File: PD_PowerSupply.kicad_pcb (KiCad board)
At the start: 4 copper layers, 61 x 46 mm, 81 parts, among them J1 2.54mm Header, J2 Screw Terminal, Q1 STL6P3LLH6, Q2 STL6P3LLH6, U1 LM1117LD-3.3, U2 STUSB4500QTR, U3 LMR16006YQ5, U4 LTM8074IY, U5 LTC7106EDDB-1, U6 LMP92064SDE_NOPB, U7 AQV252GAX, U8 BMD-340-A-R, U9 USB6B1

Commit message: Regenerate Gerbers
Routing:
- net +5V: track 89.1 -> 88.5 mm

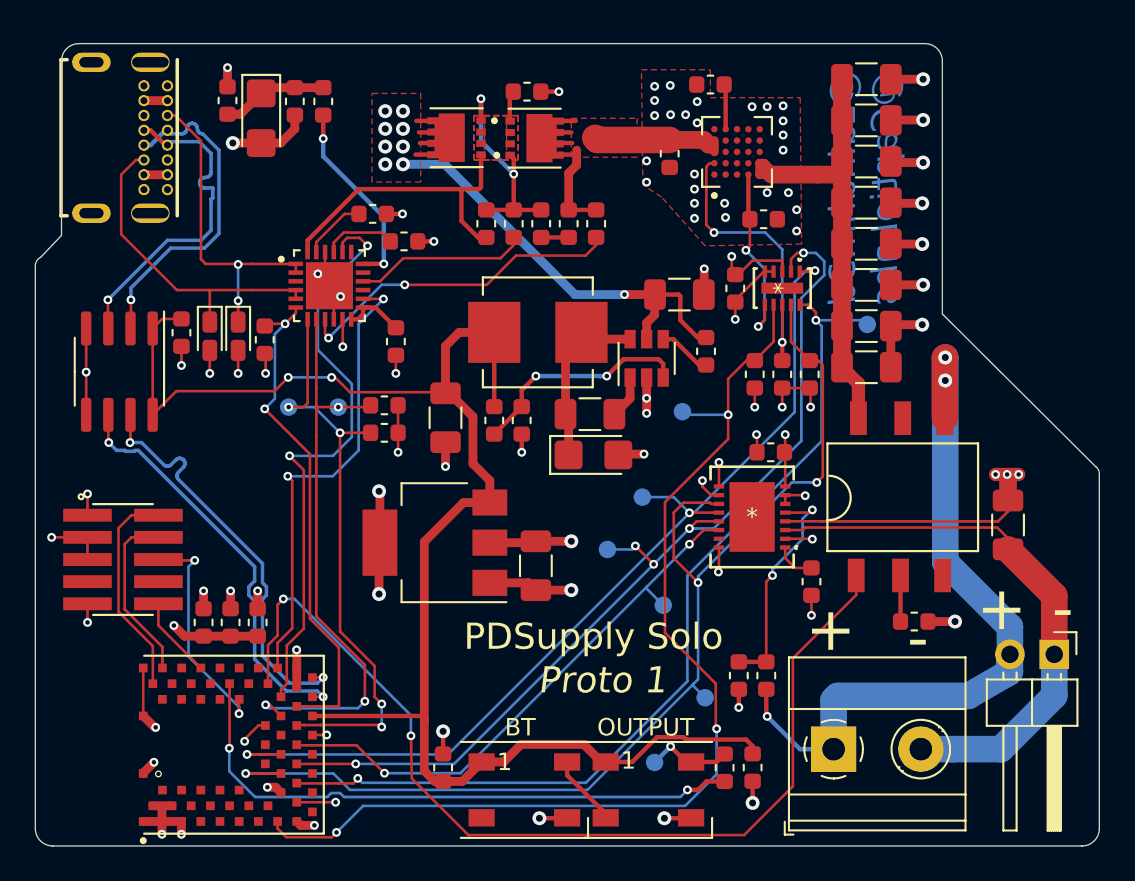
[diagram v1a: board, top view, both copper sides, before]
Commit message: Switched to PWM DAC
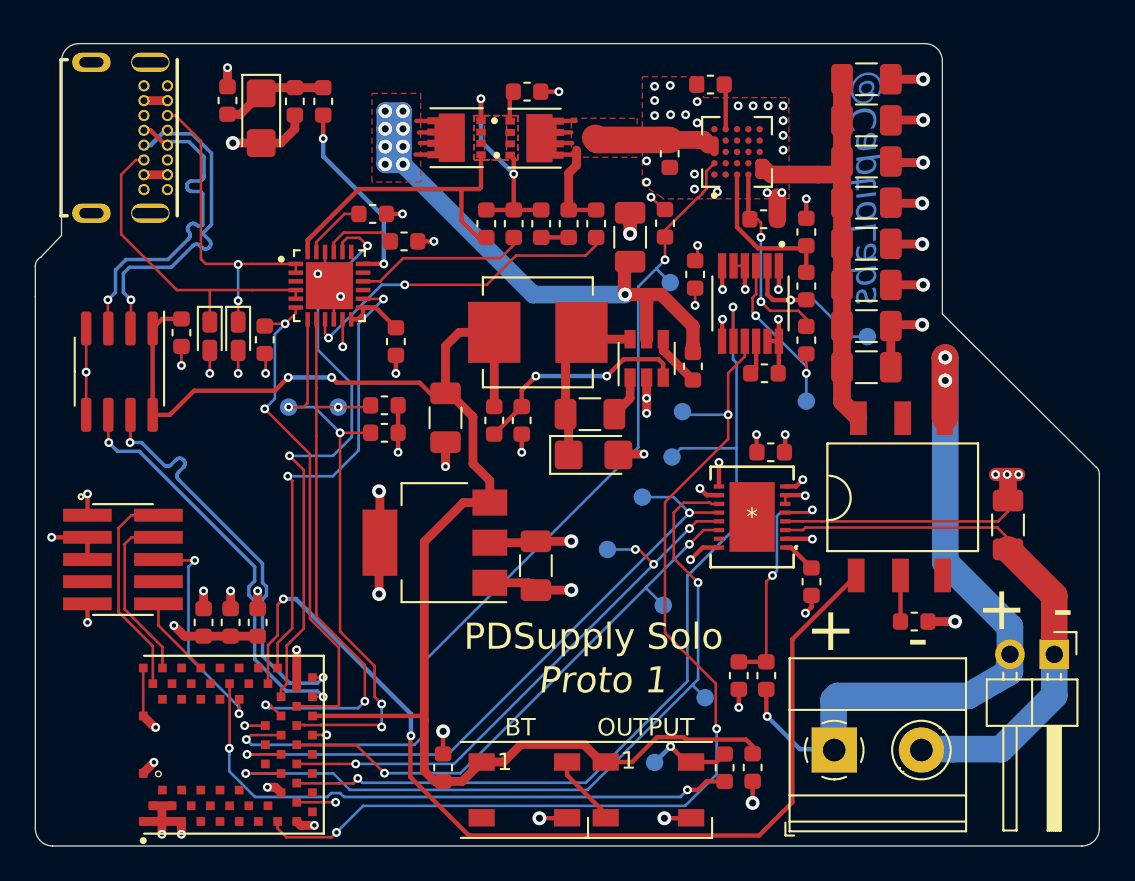
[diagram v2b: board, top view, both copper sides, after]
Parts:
- added BUCK_ENABLE1: TestPoint, TestPoint:TestPoint_Pad_D1.0mm, B.Cu at (148.5, 87.4)
- added C28: 0.1uF, Capacitor_SMD:C_0603_1608Metric, F.Cu at (153.9, 92.6)
- added DACOUTA1: TestPoint, TestPoint:TestPoint_Pad_D1.0mm, B.Cu at (159.8, 90.5)
- added DACOUTB1: TestPoint, TestPoint:TestPoint_Pad_D1.0mm, B.Cu at (156.3, 94.2)
- added R24: 9K, Resistor_SMD:R_0603_1608Metric, F.Cu at (156.3, 87.6)
- R12: value 47K -> 15k
- R15: value 10k -> DNP
- R23: value 1.1K -> 720
- R7: value 10k -> 3.5k
- U5: value LTC7106EDDB-1 -> LTC2644CMS-L10#PBF; footprint ul_LTC7106EDDB:LTC7106EDDB -> LTC2644CMS-L10_PBF:SOP65P490X110-12N_LTC2644CMS-L10#PBF
- moved DACPWMB1 13.5 mm to (148.6, 97.4)
- moved R10 11.0 mm to (148.2, 84.0), turned to 270 degrees
- moved R7 8.16 mm to (156.3, 84.5)
- moved C15 4.34 mm to (146.2, 84.8), turned to 270 degrees
- moved R15 3.55 mm to (156.3, 90.7), turned to 90 degrees
- moved C10 2.44 mm to (149.9, 87.0)
- moved U5 2.02 mm to (153.1, 88.6)
- moved R20 1.14 mm to (149.8, 92.2)
- moved J2 0.06 mm to (157.9, 114.2)
- renumbered LTC_EN1 to DACPWMA1, LTC_CSB1 to DACPWMB1
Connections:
- DACPWMA1 pad 1: /LTC7106_EN -> /DACPWMA
- DACPWMB1 pad 1: /LTC7106_CSB -> /DACPWMB
- R10 pad 2: Net-(R10-Pad2) -> /BUCK_ENABLE
- R15 pad 1: /LTC7106_EN -> Net-(DACOUTB1-Pad1)
- R15 pad 2: GND -> Net-(R12-Pad1)
- R7 pad 1: +3V3 -> Net-(R24-Pad2)
- R7 pad 2: /MISO -> GND
- U4 pad A2: Net-(R10-Pad2) -> /BUCK_ENABLE
- U4 pad C1: Net-(U4-PadC1) -> Net-(R24-Pad2)
- U5 pad 1: /MOSI -> +3V3
- U5 pad 10: /LTC7106_CSB -> Net-(C28-Pad1)
- U5 pad 11: Net-(U5-Pad11) -> GND
- U5 pad 2: /SCLK -> Net-(DACOUTA1-Pad1)
- U5 pad 3: +3V3 -> Net-(DACOUTB1-Pad1)
- U5 pad 4: GND -> +3V3
- U5 pad 5: GND -> +3V3
- U5 pad 6: Net-(R12-Pad1) -> GND
- U5 pad 7: /LTC7106_EN -> +3V3
- U5 pad 8: Net-(R10-Pad2) -> /DACPWMB
- U5 pad 9: /MISO -> /DACPWMA
- U8 pad 15: /LTC7106_EN -> /DACPWMA
- U8 pad 19: /LTC7106_CSB -> /DACPWMB
- U8 pad 24: Net-(U8-Pad24) -> /BUCK_ENABLE
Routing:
- net /LTC7106_EN: track 61.0 -> 0.00 mm, vias 3 -> 0
- net /DACPWMA: track 0.00 -> 57.9 mm, vias 0 -> 3
- net /LTC7106_CSB: track 53.8 -> 0.00 mm, vias 2 -> 0
- net /DACPWMB: track 0.00 -> 53.7 mm, vias 0 -> 2
- net /BUCK_ENABLE: track 0.00 -> 53.5 mm, vias 0 -> 2
- net /SCLK: track 55.4 -> 33.0 mm, vias 5 -> 4
- net /MISO: track 65.8 -> 45.0 mm, vias 3 -> 2
- net /MOSI: track 56.1 -> 37.9 mm, vias 3 -> 2
- net Net-(R10-Pad2): track 17.4 -> 0.00 mm, vias 2 -> 0
- net /VUSB_RAW: track 46.9 -> 58.6 mm
- net Net-(DACOUTB1-Pad1): track 0.00 -> 10.2 mm, vias 0 -> 2
- net Net-(DACOUTA1-Pad1): track 0.00 -> 9.28 mm, vias 0 -> 1
- net Net-(R24-Pad2): track 0.00 -> 9.02 mm
- net GND: track 105.3 -> 108.6 mm, vias 82 -> 80
- net +3V3: track 35.7 -> 33.2 mm, vias 13 -> 16
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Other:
- board text added: "@CaptioLabs"
- board text added: "U5"
- board text removed: "@zainahm3d @CaptioLabs"

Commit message: Added level shifter for ADC
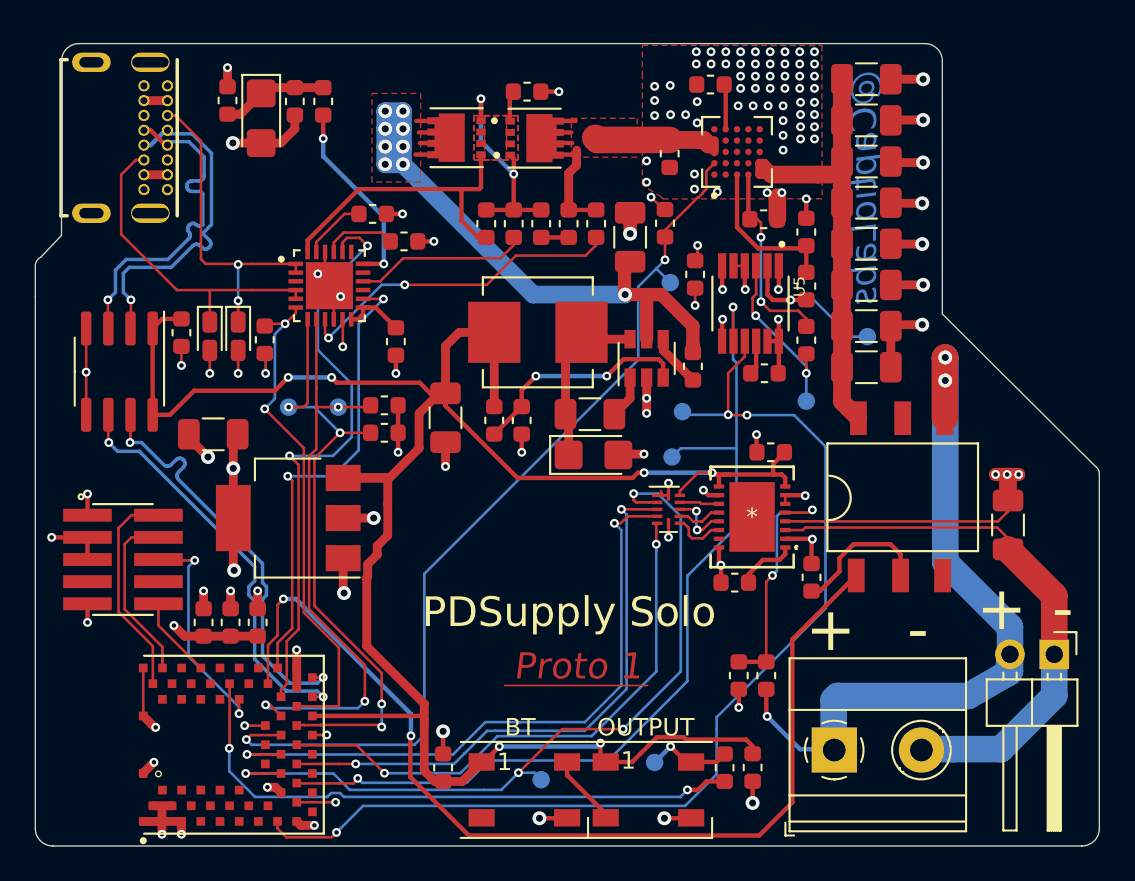
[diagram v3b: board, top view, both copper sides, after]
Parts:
- removed LMP_CSB1, MOSI1, SCLK1: TestPoint, TestPoint:TestPoint_Pad_D1.0mm
- added U10: TXB0104RUT, Package_DFN_QFN:Texas_R_PUQFN-N12, F.Cu at (148.4, 100.4)
- R24: value 9K -> 10k
- R7: value 3.5k -> 3.9k
- moved C18 20.0 mm to (122.3, 96.1), turned to 180 degrees
- moved MISO1 10.5 mm to (141.1, 115.9)
- moved U1 8.52 mm to (126.6, 100.9)
- moved R23 6.41 mm to (156.6, 104.3), turned to 90 degrees
- moved C13 4.40 mm to (152.2, 104.6), turned to 180 degrees
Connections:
- C14 pad 1: +3V3 -> +5V
- U6 pad 11: /MISO -> Net-(U10-Pad10)
- U6 pad 12: /MOSI -> Net-(U10-Pad8)
- U6 pad 13: /SCLK -> Net-(U10-Pad9)
- U6 pad 14: /LMP92064_CSB -> Net-(U10-Pad7)
- U6 pad 8: +3V3 -> +5V
- U6 pad 9: +3V3 -> +5V
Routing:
- net +5V: track 88.7 -> 122.0 mm, vias 2 -> 6
- net Net-(R23-Pad1): track 2.64 -> 8.11 mm
- net /DACPWMA: track 57.9 -> 62.3 mm
- net Net-(U10-Pad9): track 0.00 -> 3.54 mm, vias 0 -> 2
- net +3V3: track 33.2 -> 30.2 mm, vias 16 -> 14
- net Net-(U10-Pad7): track 0.00 -> 3.03 mm
- net Net-(U10-Pad8): track 0.00 -> 2.58 mm
- net Net-(U10-Pad10): track 0.00 -> 2.30 mm
- net GND: track 108.6 -> 107.0 mm, vias 80 -> 118
- net Net-(C13-Pad1): track 1.99 -> 3.44 mm
- net /I2C_SCL: track 34.3 -> 35.5 mm
- net /MOSI: track 37.9 -> 37.2 mm
- net /MISO: track 45.0 -> 45.5 mm, vias 2 -> 4
- net /SCLK: track 33.0 -> 33.2 mm, vias 4 -> 2

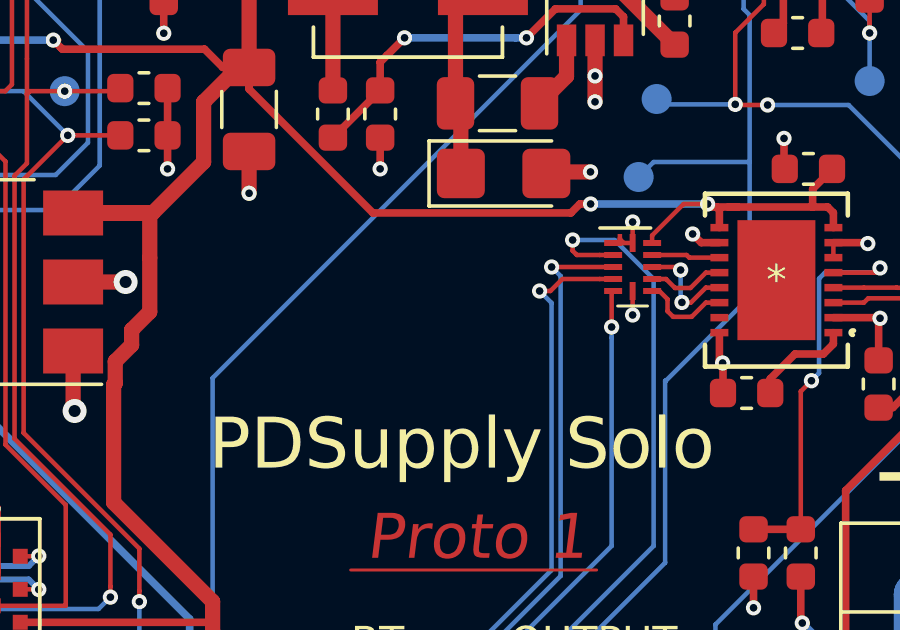
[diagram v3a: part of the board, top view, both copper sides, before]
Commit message: Added missing SPI test points (oops)
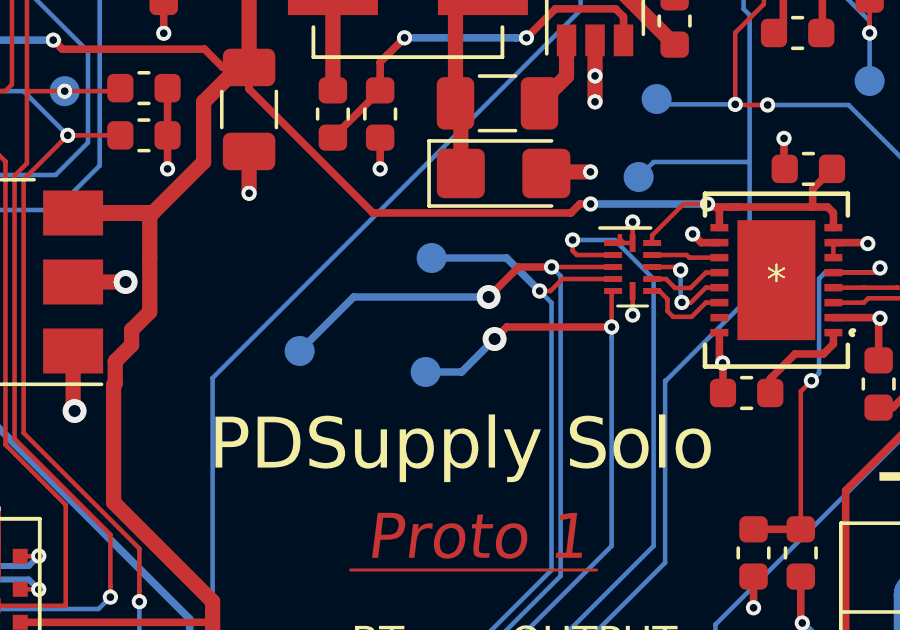
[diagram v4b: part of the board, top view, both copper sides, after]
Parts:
- added LMP_CSB1: TestPoint, TestPoint:TestPoint_Pad_D1.0mm, B.Cu at (141.5, 103.9)
- added MOSI1: TestPoint, TestPoint:TestPoint_Pad_D1.0mm, B.Cu at (141.7, 100.1)
- added SCLK1: TestPoint, TestPoint:TestPoint_Pad_D1.0mm, B.Cu at (137.3, 103.2)
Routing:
- net /SCLK: track 33.2 -> 42.7 mm, vias 2 -> 3
- net /LMP92064_CSB: track 32.2 -> 39.0 mm, vias 2 -> 3
- net /MOSI: track 37.2 -> 41.2 mm

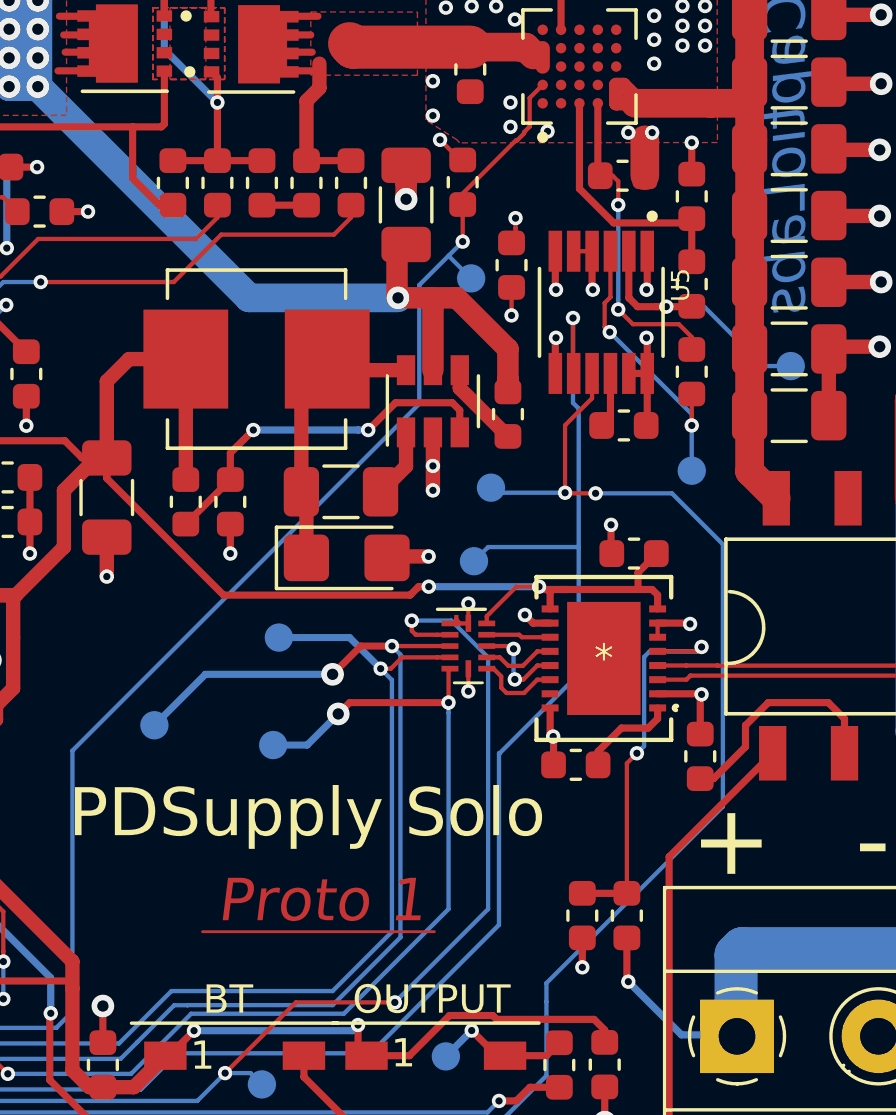
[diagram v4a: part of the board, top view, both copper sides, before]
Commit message: after testing, removed FB resistors and backup PWM DAC channel
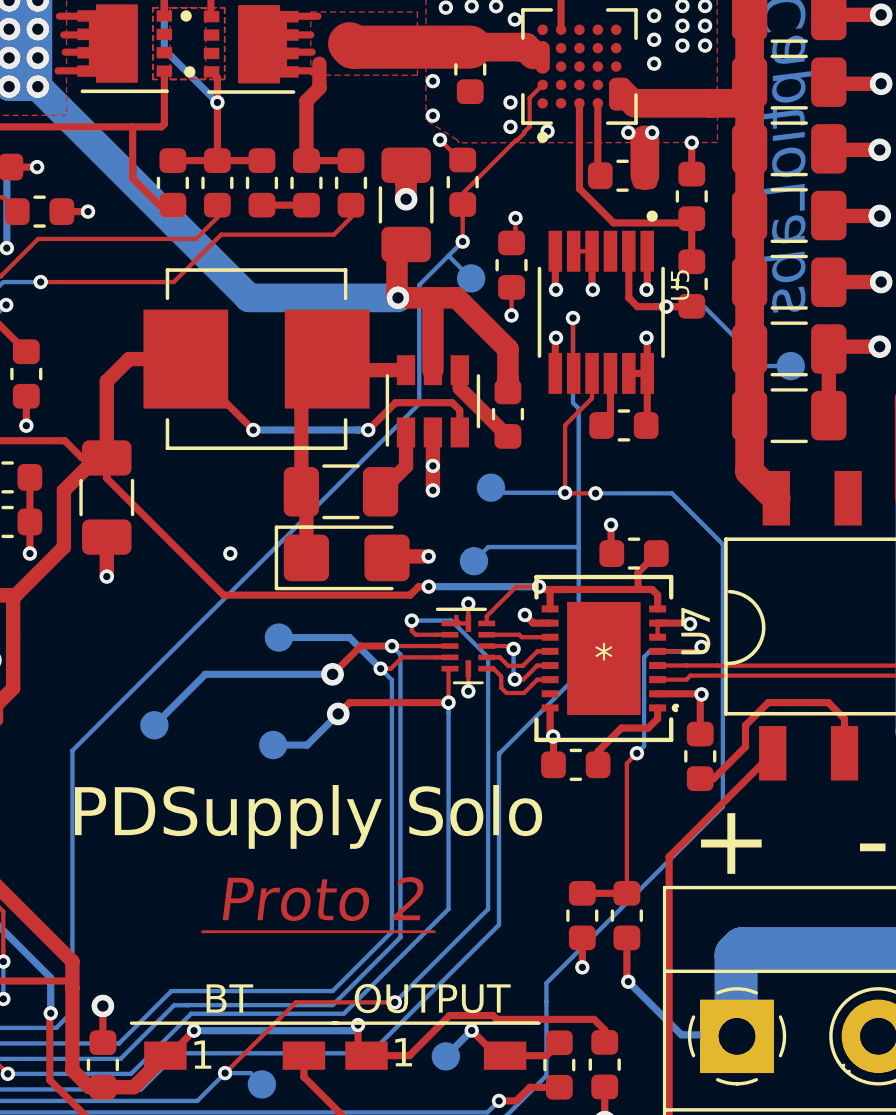
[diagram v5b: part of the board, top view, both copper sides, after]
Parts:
- removed DACOUTB1: TestPoint, TestPoint:TestPoint_Pad_D1.0mm
- removed R15: DNP, Resistor_SMD:R_0603_1608Metric
- removed R21: 54.9K, Resistor_SMD:R_0603_1608Metric
- removed R22: 10K, Resistor_SMD:R_0603_1608Metric
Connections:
- U3 pad 3: Net-(R21-Pad2) -> +5V
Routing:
- net Net-(R21-Pad2): track 12.9 -> 0.00 mm, vias 2 -> 0
- net Net-(U5-Pad3): track 10.2 -> 0.00 mm, vias 2 -> 0
- net Net-(R12-Pad1): track 11.3 -> 2.47 mm, vias 2 -> 0
- net +5V: track 122.0 -> 129.9 mm, vias 6 -> 8
- net GND: track 107.0 -> 105.9 mm
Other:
- board text added: "Proto 2"

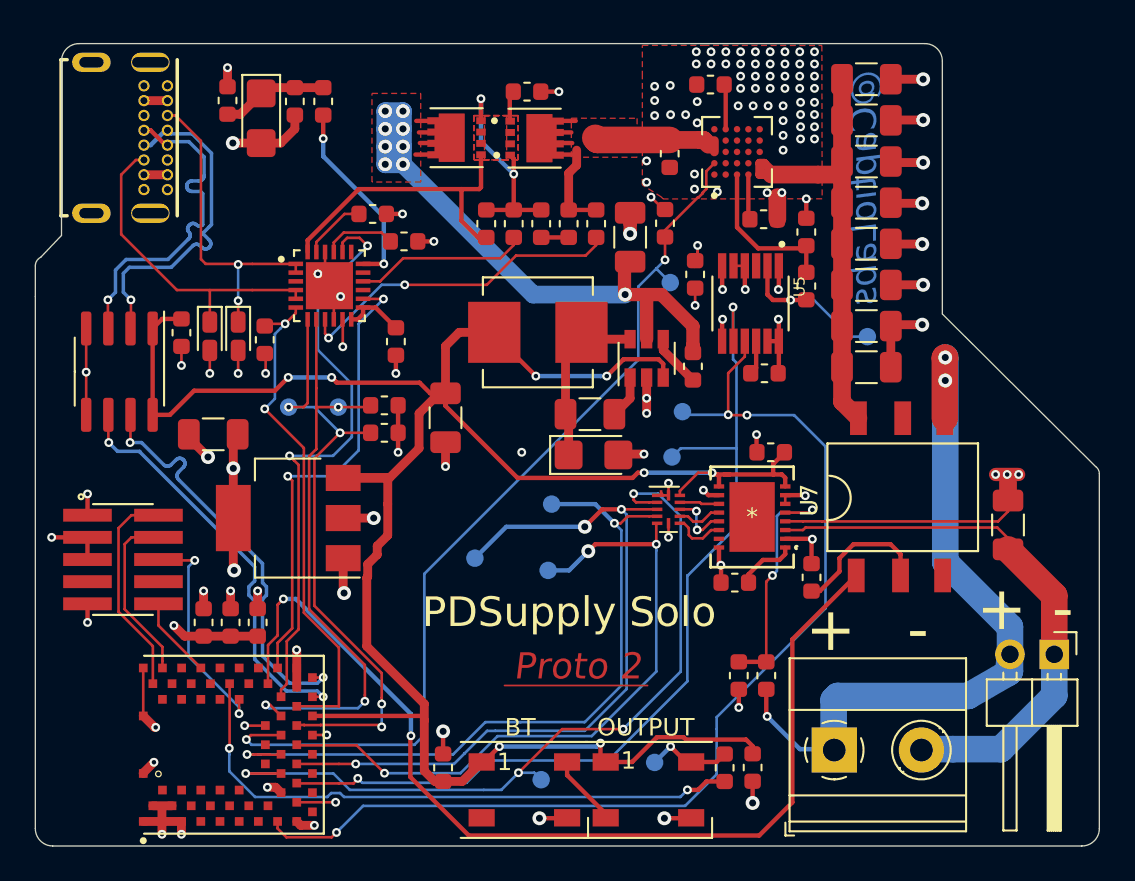
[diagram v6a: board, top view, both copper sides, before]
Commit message: [WIP] fixing voltage leakage on USB C port
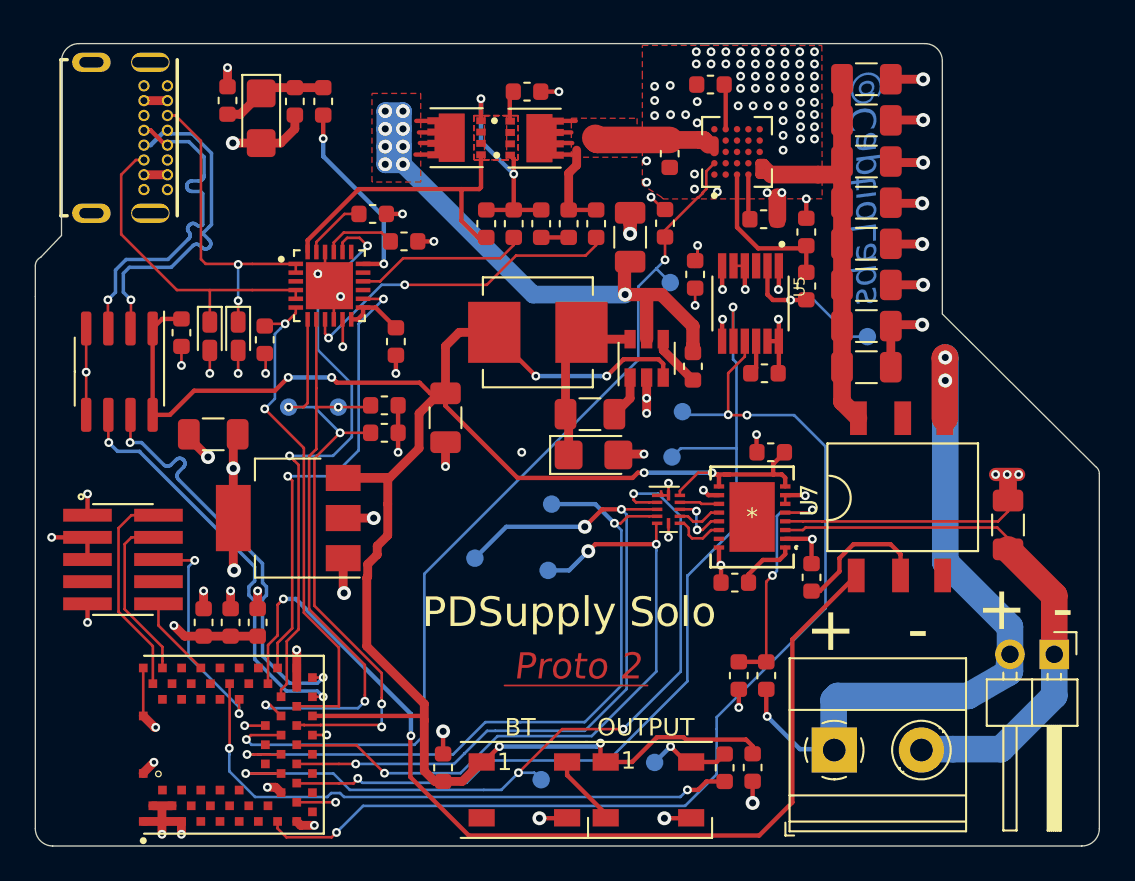
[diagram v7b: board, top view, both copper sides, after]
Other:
- outline, holes or cut-outs redrawn
- net class Default removed
- rule pad_to_mask_clearance: 0.051 -> 0
- board text removed: "Proto 1"
